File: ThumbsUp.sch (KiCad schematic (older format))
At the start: 152 parts, among them IC1 RP2040, IC2 W25Q128JVSIM, IC3 RP2040, IC4 W25Q128JVSIM, J1 Conn_01x04_Male, J10 Raiser_Male, J11 Raiser_Female, J12 Raiser_Male, J13 Raiser_Female, J14 Raiser_Male, J15 Raiser_Female, J16 Raiser_Male, J17 Raiser_Female, J18 Raiser_Male, J19 Raiser_Female, J2 Conn_01x04_Male, J20 Conn_01x04_Female, J21 Conn_01x04_Female, J22 Conn_01x04_Female, J23 Conn_01x04_Female, J24 Conn_01x04_Male, J25 Conn_01x04_Male, J26 Conn_01x04_Male, J27 Conn_01x04_Male, J28 Conn_01x04_Female, J29 Conn_01x04_Female, J3 Conn_01x04_Female, J30 Conn_01x04_Female, J31 Conn_01x04_Female, J32 USB_C_Receptacle_USB2.0, J33 Raiser_Male, J34 Raiser_Female, J35 Raiser_Male, J36 STX-3501-3N, J37 USB_C_Receptacle_USB2.0, J38 Raiser_Female, J39 Raiser_Male, J4 Conn_01x04_Male, J40 Raiser_Female, J41 Raiser_Male, J42 Raiser_Female, J43 Raiser_Male, J44 Raiser_Female, J45 Raiser_Male, J46 STX-3501-3N, J47 Raiser_Female, J48 Raiser_Male, J5 Conn_01x04_Female, J6 Conn_01x04_Male, J7 Conn_01x04_Male, J8 Conn_01x04_Male, J9 Raiser_Female, U1 NCP1117-3.3_SOT223, U2 NCP1117-3.3_SOT223, Y1 ABLS-12.000MHZ-B4-T, Y2 ABLS-12.000MHZ-B4-T

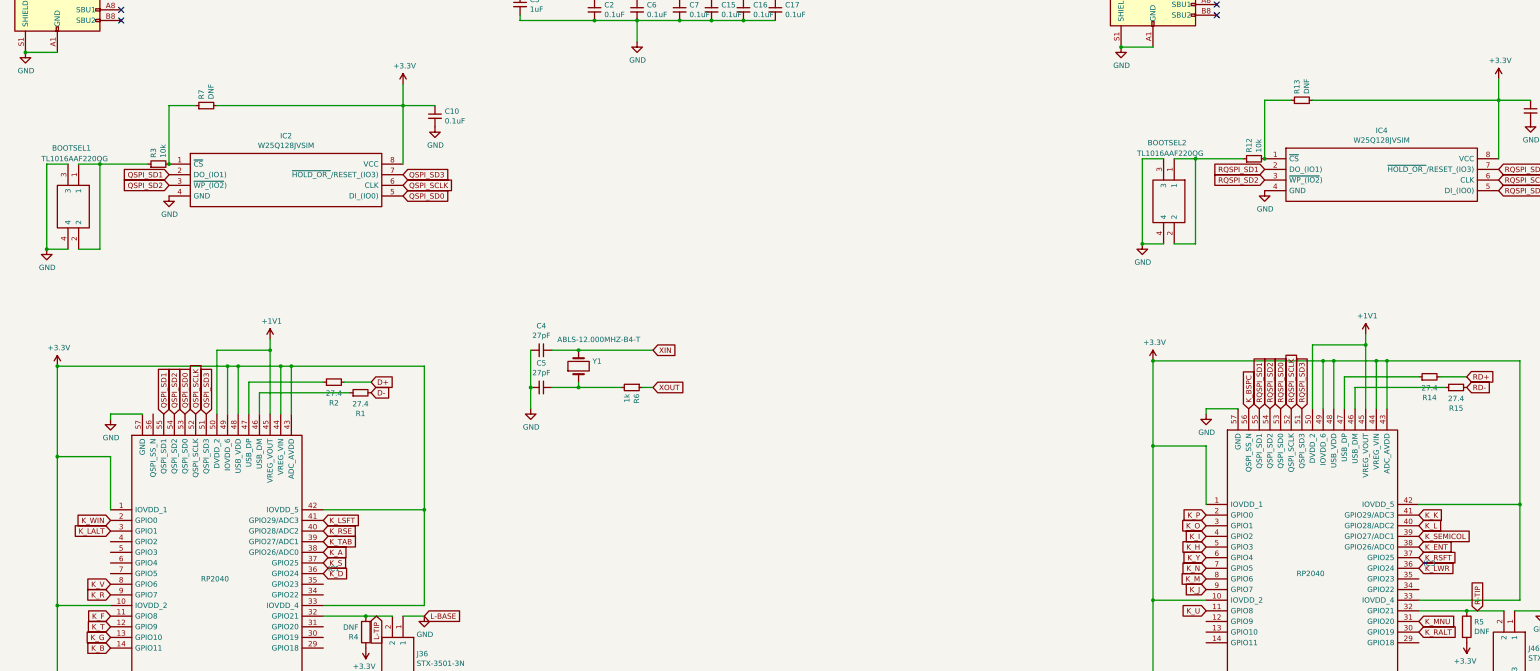
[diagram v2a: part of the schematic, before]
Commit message: Added a missing line SS-N
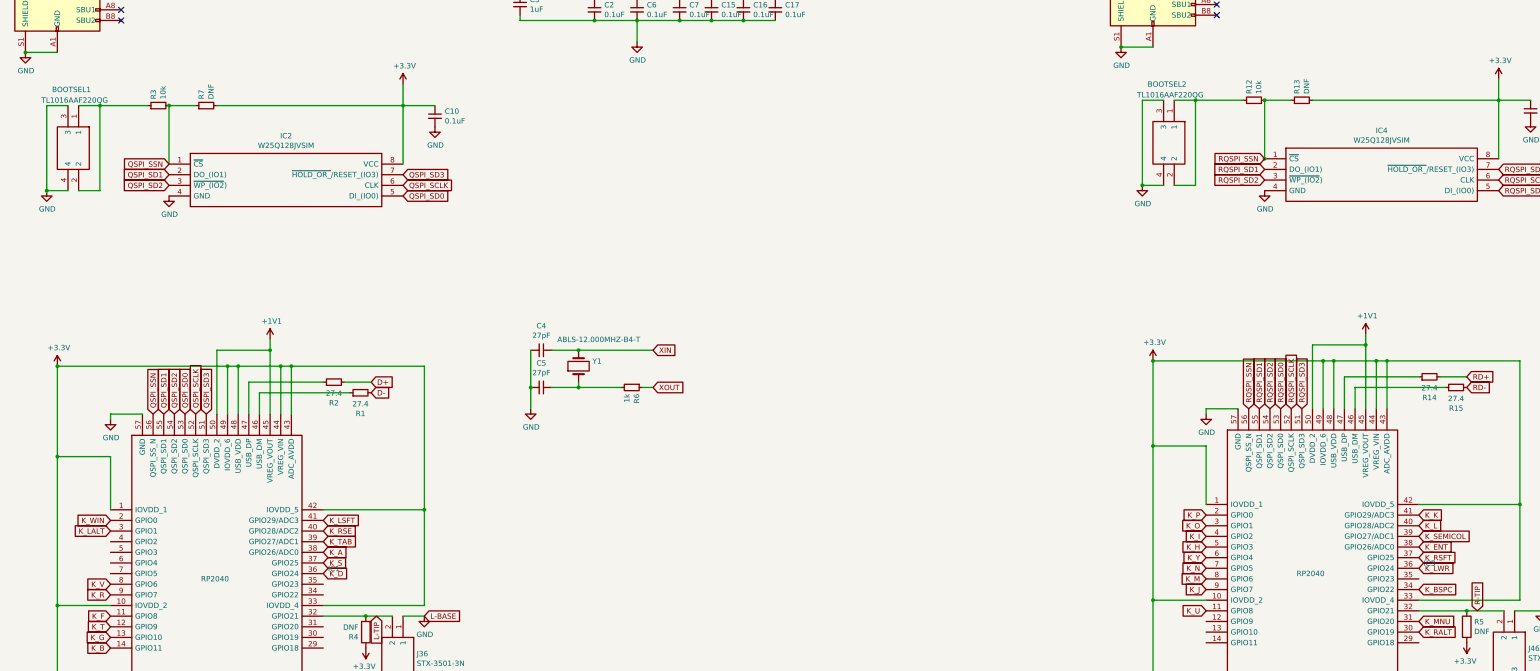
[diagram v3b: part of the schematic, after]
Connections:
- net K_BSPC: now also IC3.34 (GPIO22); no longer IC3.56 (QSPI_SS_N)
- net QSPI_SSN: now reaches IC2.1 (~CS), R3.2, R7.1
- net QSPI_SSN: now also IC1.56 (QSPI_SS_N)
- net RQSPI_SSN: now reaches IC4.1 (~CS), R12.2, R13.1
- net RQSPI_SSN: now also IC3.56 (QSPI_SS_N)
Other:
- moved on the sheet: BOOTSEL1, BOOTSEL2, R12, R3
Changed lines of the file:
@@
 L Device:R_Small R3
 U 1 1 616D4E45
-P 2700 3850
-F 0 "R3" H 2759 3896 50  0000 L CNN
-F 1 "10k" H 2759 3805 50  0000 L CNN
-F 2 "Resistor_SMD:R_0402_1005Metric" H 2700 3850 50  0001 C CNN
-F 3 "~" H 2700 3850 50  0001 C CNN
-	1    2700 3850
+P 2700 3300
+F 0 "R3" H 2759 3346 50  0000 L CNN
+F 1 "10k" H 2759 3255 50  0000 L CNN
+F 2 "Resistor_SMD:R_0402_1005Metric" H 2700 3300 50  0001 C CNN
+F 3 "~" H 2700 3300 50  0001 C CNN
+	1    2700 3300
 	0    -1   -1   0
 $EndComp
@@
 Wire Wire Line
 	2800 3300 3050 3300
-Connection ~ 2800 3850
 Text GLabel 5000 4150 2    50   Input ~ 0
 QSPI_SD0
@@
 L TL1016AAF220QG:TL1016AAF220QG BOOTSEL1
 U 1 1 63B7CD0C
-P 1950 3850
-F 0 "BOOTSEL1" V 1800 3600 50  0000 L CNN
-F 1 "TL1016AAF220QG" V 1900 3500 50  0000 L CNN
-F 2 "TL1016AAF220QG:TL1016AAF220QG" H 2600 3950 50  0001 L CNN
-F 3 "https://eu.mouser.com/datasheet/2/140/E_Switch_05112022_TL1016_Datasheet-2943618.pdf" H 2600 3850 50  0001 L CNN
-F 4 "Tactile Switches Tactile Switch SPST OFF-(ON) 50mA 12VDC" H 2600 3750 50  0001 L CNN "Description"
-F 5 "1.35" H 2600 3650 50  0001 L CNN "Height"
-F 6 "E-Switch" H 2600 3550 50  0001 L CNN "Manufacturer_Name"
-F 7 "TL1016AAF220QG" H 2600 3450 50  0001 L CNN "Manufacturer_Part_Number"
-F 8 "612-TL1016AAF220QG" H 2600 3350 50  0001 L CNN "Mouser Part Number"
-F 9 "https://www.mouser.co.uk/ProductDetail/E-Switch/TL1016AAF220QG?qs=t7xnP681wgW5zrSpkWH91Q%3D%3D" H 2600 3250 50  0001 L CNN "Mouser Price/Stock"
-F 10 "" H 2600 3150 50  0001 L CNN "Arrow Part Number"
-F 11 "" H 2600 3050 50  0001 L CNN "Arrow Price/Stock"
-F 12 "" H 2600 2950 50  0001 L CNN "Mouser Testing Part Number"
-F 13 "" H 2600 2850 50  0001 L CNN "Mouser Testing Price/Stock"
-	1    1950 3850
+P 1950 3300
+F 0 "BOOTSEL1" V 1800 3050 50  0000 L CNN
+F 1 "TL1016AAF220QG" V 1900 2950 50  0000 L CNN
+F 2 "TL1016AAF220QG:TL1016AAF220QG" H 2600 3400 50  0001 L CNN
+F 3 "https://eu.mouser.com/datasheet/2/140/E_Switch_05112022_TL1016_Datasheet-2943618.pdf" H 2600 3300 50  0001 L CNN
+F 4 "Tactile Switches Tactile Switch SPST OFF-(ON) 50mA 12VDC" H 2600 3200 50  0001 L CNN "Description"
+F 5 "1.35" H 2600 3100 50  0001 L CNN "Height"
+F 6 "E-Switch" H 2600 3000 50  0001 L CNN "Manufacturer_Name"
+F 7 "TL1016AAF220QG" H 2600 2900 50  0001 L CNN "Manufacturer_Part_Number"
+F 8 "612-TL1016AAF220QG" H 2600 2800 50  0001 L CNN "Mouser Part Number"
+F 9 "https://www.mouser.co.uk/ProductDetail/E-Switch/TL1016AAF220QG?qs=t7xnP681wgW5zrSpkWH91Q%3D%3D" H 2600 2700 50  0001 L CNN "Mouser Price/Stock"
+F 10 "" H 2600 2600 50  0001 L CNN "Arrow Part Number"
+F 11 "" H 2600 2500 50  0001 L CNN "Arrow Price/Stock"
+F 12 "" H 2600 2400 50  0001 L CNN "Mouser Testing Part Number"
+F 13 "" H 2600 2300 50  0001 L CNN "Mouser Testing Price/Stock"
+	1    1950 3300
 	0    1    1    0
 $EndComp
 Wire Wire Line
-	1950 3850 2150 3850
+	1950 3300 2150 3300
 Wire Wire Line
-	1950 4650 2150 4650
+	1950 4100 2150 4100
 Wire Wire Line
-	2150 4650 2150 3850
-Connection ~ 2150 3850
+	2150 4100 2150 3300
+Connection ~ 2150 3300
 Wire Wire Line
-	2150 3850 2600 3850
+	2150 3300 2600 3300
 Wire Wire Line
-	1850 3850 1650 3850
+	1850 3300 1650 3300
 Wire Wire Line
-	1650 3850 1650 4650
+	1650 3300 1650 4100
 Wire Wire Line
-	1650 4650 1850 4650
+	1650 4100 1850 4100
 $Comp
 L power:GND #PWR0120
 U 1 1 63D2EFAD
-P 1650 4650
-F 0 "#PWR0120" H 1650 4400 50  0001 C CNN
-F 1 "GND" H 1655 4477 50  0000 C CNN
-F 2 "" H 1650 4650 50  0001 C CNN
-F 3 "" H 1650 4650 50  0001 C CNN
-	1    1650 4650
+P 1650 4100
+F 0 "#PWR0120" H 1650 3850 50  0001 C CNN
+F 1 "GND" H 1655 3927 50  0000 C CNN
+F 2 "" H 1650 4100 50  0001 C CNN
+F 3 "" H 1650 4100 50  0001 C CNN
+	1    1650 4100
 	1    0    0    -1
 $EndComp
-Connection ~ 1650 4650
+Connection ~ 1650 4100
 Wire Wire Line
 	1750 9650 1750 8000
@@
 L Device:R_Small R12
 U 1 1 63C3379F
-P 13000 3800
-F 0 "R12" H 13059 3846 50  0000 L CNN
-F 1 "10k" H 13059 3755 50  0000 L CNN
-F 2 "Resistor_SMD:R_0402_1005Metric" H 13000 3800 50  0001 C CNN
-F 3 "~" H 13000 3800 50  0001 C CNN
-	1    13000 3800
+P 13000 3250
+F 0 "R12" H 13059 3296 50  0000 L CNN
+F 1 "10k" H 13059 3205 50  0000 L CNN
+F 2 "Resistor_SMD:R_0402_1005Metric" H 13000 3250 50  0001 C CNN
+F 3 "~" H 13000 3250 50  0001 C CNN
+	1    13000 3250
 	0    -1   -1   0
 $EndComp
@@
 L TL1016AAF220QG:TL1016AAF220QG BOOTSEL2
 U 1 1 63C3393B
-P 12250 3800
-F 0 "BOOTSEL2" V 12100 3550 50  0000 L CNN
-F 1 "TL1016AAF220QG" V 12200 3450 50  0000 L CNN
-F 2 "TL1016AAF220QG:TL1016AAF220QG" H 12900 3900 50  0001 L CNN
-F 3 "https://eu.mouser.com/datasheet/2/140/E_Switch_05112022_TL1016_Datasheet-2943618.pdf" H 12900 3800 50  0001 L CNN
-F 4 "Tactile Switches Tactile Switch SPST OFF-(ON) 50mA 12VDC" H 12900 3700 50  0001 L CNN "Description"
-F 5 "1.35" H 12900 3600 50  0001 L CNN "Height"
-F 6 "E-Switch" H 12900 3500 50  0001 L CNN "Manufacturer_Name"
-F 7 "TL1016AAF220QG" H 12900 3400 50  0001 L CNN "Manufacturer_Part_Number"
-F 8 "612-TL1016AAF220QG" H 12900 3300 50  0001 L CNN "Mouser Part Number"
-F 9 "https://www.mouser.co.uk/ProductDetail/E-Switch/TL1016AAF220QG?qs=t7xnP681wgW5zrSpkWH91Q%3D%3D" H 12900 3200 50  0001 L CNN "Mouser Price/Stock"
-F 10 "" H 12900 3100 50  0001 L CNN "Arrow Part Number"
-F 11 "" H 12900 3000 50  0001 L CNN "Arrow Price/Stock"
-F 12 "" H 12900 2900 50  0001 L CNN "Mouser Testing Part Number"
-F 13 "" H 12900 2800 50  0001 L CNN "Mouser Testing Price/Stock"
-	1    12250 3800
+P 12250 3250
+F 0 "BOOTSEL2" V 12100 3000 50  0000 L CNN
+F 1 "TL1016AAF220QG" V 12200 2900 50  0000 L CNN
+F 2 "TL1016AAF220QG:TL1016AAF220QG" H 12900 3350 50  0001 L CNN
+F 3 "https://eu.mouser.com/datasheet/2/140/E_Switch_05112022_TL1016_Datasheet-2943618.pdf" H 12900 3250 50  0001 L CNN
+F 4 "Tactile Switches Tactile Switch SPST OFF-(ON) 50mA 12VDC" H 12900 3150 50  0001 L CNN "Description"
+F 5 "1.35" H 12900 3050 50  0001 L CNN "Height"
+F 6 "E-Switch" H 12900 2950 50  0001 L CNN "Manufacturer_Name"
+F 7 "TL1016AAF220QG" H 12900 2850 50  0001 L CNN "Manufacturer_Part_Number"
+F 8 "612-TL1016AAF220QG" H 12900 2750 50  0001 L CNN "Mouser Part Number"
+F 9 "https://www.mouser.co.uk/ProductDetail/E-Switch/TL1016AAF220QG?qs=t7xnP681wgW5zrSpkWH91Q%3D%3D" H 12900 2650 50  0001 L CNN "Mouser Price/Stock"
+F 10 "" H 12900 2550 50  0001 L CNN "Arrow Part Number"
+F 11 "" H 12900 2450 50  0001 L CNN "Arrow Price/Stock"
+F 12 "" H 12900 2350 50  0001 L CNN "Mouser Testing Part Number"
+F 13 "" H 12900 2250 50  0001 L CNN "Mouser Testing Price/Stock"
+	1    12250 3250
 	0    1    1    0
 $EndComp
 Wire Wire Line
-	12250 3800 12450 3800
+	12250 3250 12450 3250
 Wire Wire Line
-	12250 4600 12450 4600
+	12250 4050 12450 4050
 Wire Wire Line
-	12450 4600 12450 3800
-Connection ~ 12450 3800
+	12450 4050 12450 3250
+Connection ~ 12450 3250
 Wire Wire Line
-	12450 3800 12900 3800
+	12450 3250 12900 3250
 Wire Wire Line
-	12150 3800 11950 3800
+	12150 3250 11950 3250
 Wire Wire Line
-	11950 3800 11950 4600
+	11950 3250 11950 4050
 Wire Wire Line
-	11950 4600 12150 4600
+	11950 4050 12150 4050
 $Comp
 L power:GND #PWR0144
 U 1 1 63C33949
-P 11950 4600
-F 0 "#PWR0144" H 11950 4350 50  0001 C CNN
-F 1 "GND" H 11955 4427 50  0000 C CNN
-F 2 "" H 11950 4600 50  0001 C CNN
-F 3 "" H 11950 4600 50  0001 C CNN
-	1    11950 4600
+P 11950 4050
+F 0 "#PWR0144" H 11950 3800 50  0001 C CNN
+F 1 "GND" H 11955 3877 50  0000 C CNN
+F 2 "" H 11950 4050 50  0001 C CNN
+F 3 "" H 11950 4050 50  0001 C CNN
+	1    11950 4050
 	1    0    0    -1
 $EndComp
-Connection ~ 11950 4600
+Connection ~ 11950 4050
 $Comp
 L Device:R_Small R11
@@
 Wire Wire Line
 	14550 8050 15000 8050
-Text GLabel 12950 6150 1    50   Input ~ 0
+Text GLabel 14550 7850 2    50   Input ~ 0
 K_BSPC
 Text GLabel 12550 7150 0    50   Input ~ 0
@@
 Text GLabel 2250 7300 0    50   Input ~ 0
 K_LALT
+Text GLabel 2650 6200 1    50   Input ~ 0
+QSPI_SSN
+Connection ~ 2800 3300
+Text GLabel 2800 3850 0    50   Input ~ 0
+QSPI_SSN
+Connection ~ 13100 3250
+Text GLabel 12950 6150 1    50   Input ~ 0
+RQSPI_SSN
+Text GLabel 13100 3800 0    50   Input ~ 0
+RQSPI_SSN
 $EndSCHEMATC

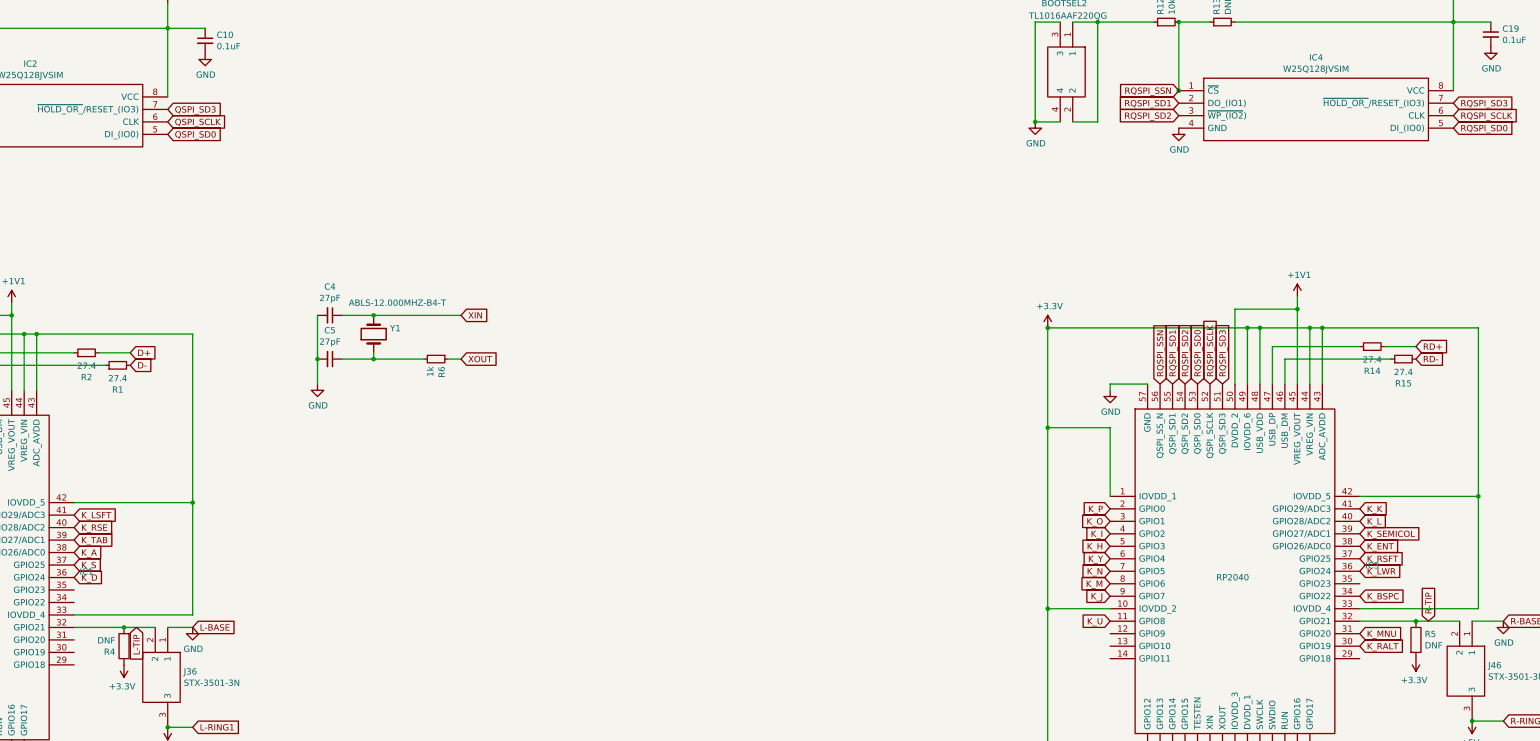
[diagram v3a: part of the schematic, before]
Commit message: Added BOM, fixed the placement files
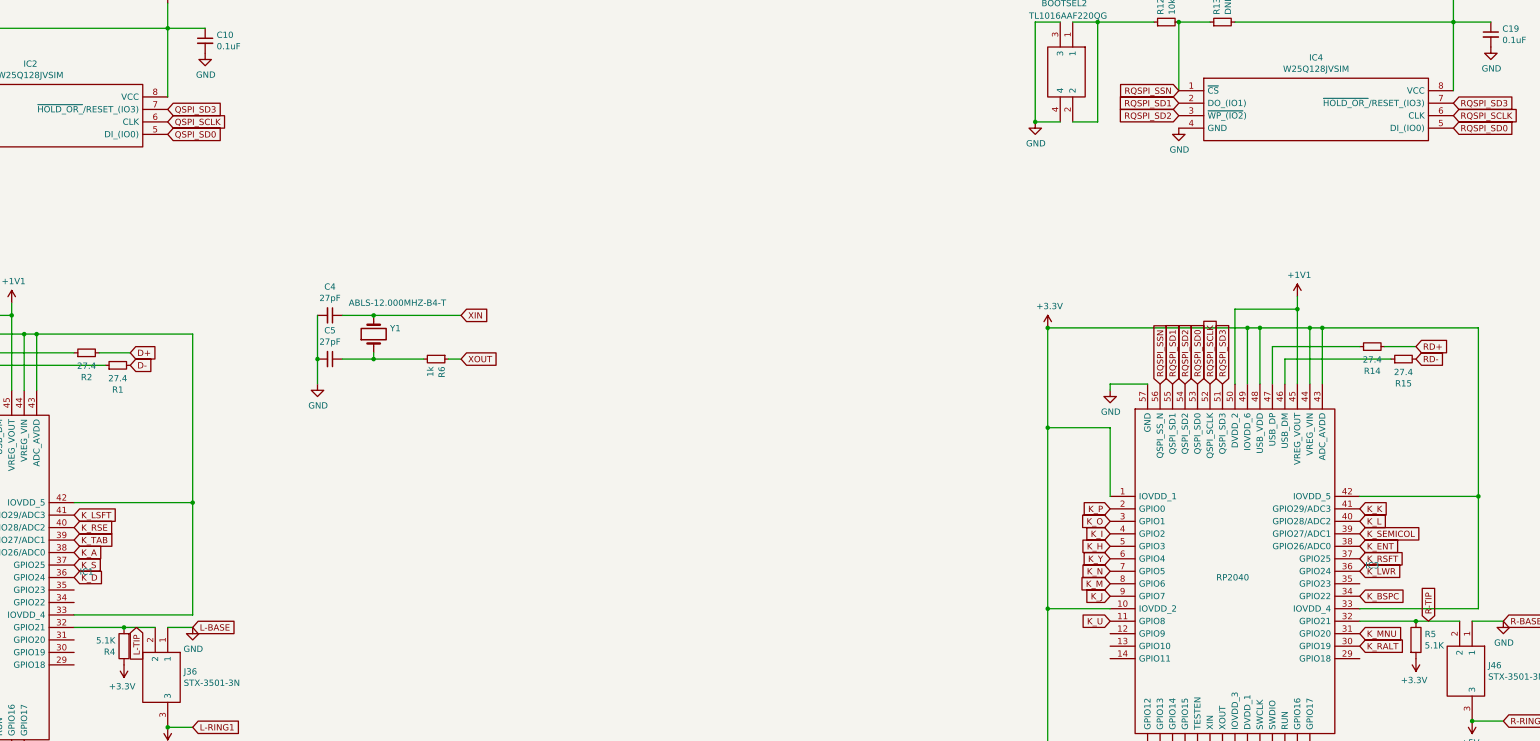
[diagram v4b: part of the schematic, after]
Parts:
- R4, R5: value DNF -> 5.1K
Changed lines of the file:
@@
 Wire Wire Line
 	13100 3250 13350 3250
-Connection ~ 13100 3800
 $Comp
 L power:GND #PWR0142
@@
 P 4650 8250
 F 0 "R4" H 4720 8296 50  0000 L CNN
-F 1 "DNF" H 4720 8205 50  0000 L CNN
+F 1 "5.1K" H 4720 8205 50  0000 L CNN
 F 2 "Resistor_SMD:R_0805_2012Metric" V 4580 8250 50  0001 C CNN
 F 3 "~" H 4650 8250 50  0001 C CNN
@@
 P 15000 8200
 F 0 "R5" H 15070 8246 50  0000 L CNN
-F 1 "DNF" H 15070 8155 50  0000 L CNN
+F 1 "5.1K" H 15070 8155 50  0000 L CNN
 F 2 "Resistor_SMD:R_0805_2012Metric" V 14930 8200 50  0001 C CNN
 F 3 "~" H 15000 8200 50  0001 C CNN
